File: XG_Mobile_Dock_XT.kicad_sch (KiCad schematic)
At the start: 101 parts, among them J1 5-1775443-8, J13 39301240, J14 I2C1, J2 20455-040E-76, J3 20455-040E-76, J5 USB_C_Receptacle, J6 455860005, SW1 SW_Push, U1 DS320PR810NJXR, U2 DS320PR810NJXR

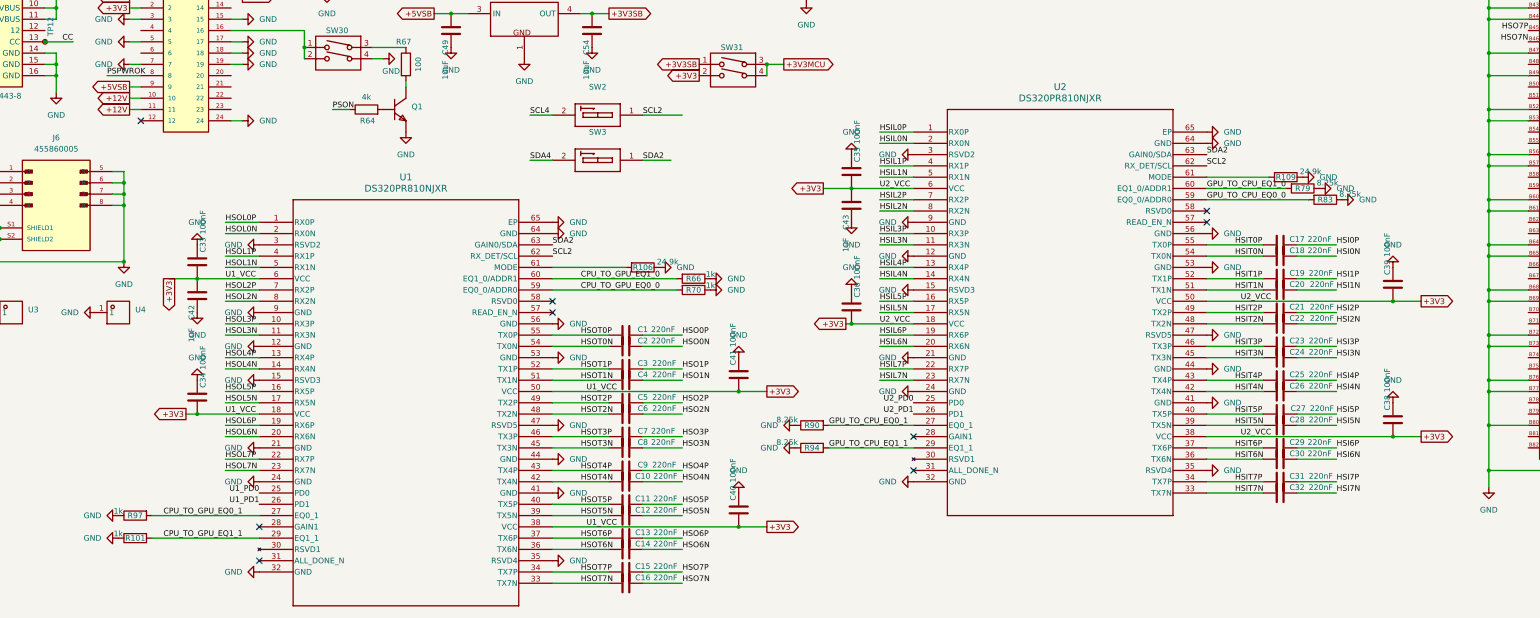
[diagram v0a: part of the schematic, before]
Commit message: moved redrivers in separate schematic
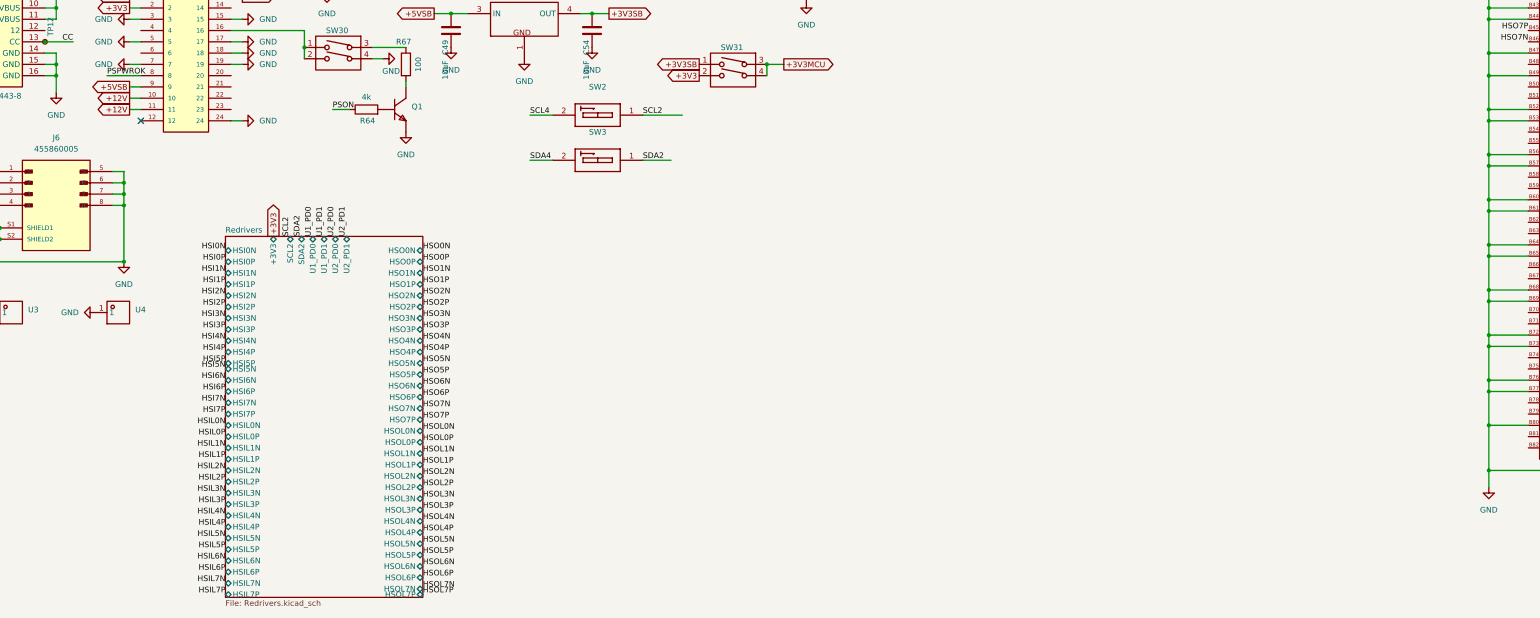
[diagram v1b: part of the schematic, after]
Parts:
- removed C1, C10, C11, C12, C13, C14, C15, C16, C17, C18, C19, C2, C20, C21, C22, C23, C24, C25, C26, C27, C28, C29, C3, C30, C31, C32, C4, C5, C6, C7, C8, C9: 220nF, Capacitor_SMD:C_0201_0603Metric, symbol Device:C
- removed C33, C34, C35, C36, C38, C39, C40, C41: 100nF, Capacitor_SMD:C_0201_0603Metric, symbol Device:C
- removed C42, C43: 1uF, Capacitor_SMD:C_0201_0603Metric, symbol Device:C
- removed R101, R66, R70, R97: 1k, Resistor_SMD:R_0603_1608Metric, symbol Device:R
- removed R106, R109: 24.9k, Resistor_SMD:R_0603_1608Metric, symbol Device:R
- removed R79, R83, R90, R94: 8.25k, Resistor_SMD:R_0603_1608Metric, symbol Device:R
- removed U1, U2: DS320PR810NJXR, WQFN-64-NJX_TEX, symbol DS320PR810NJXR:DS320PR810NJXR
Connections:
- no-connect marks 9 -> 1
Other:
- added sheet Redrivers (Redrivers.kicad_sch)
